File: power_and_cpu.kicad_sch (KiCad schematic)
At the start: 242 parts, among them J1 CPU1 USB, J10 AUX GPIO 1, J11 CAN2 PLUG, J12 Conn_01x06, J13 ADC AUX 2, J14 AUX GPIO 2, J15 AUX Encoder, J17 CAN Output, J2 CAN Input, J21 Power Input, J3 Encoder 1, J4 Encoder 2, J5 Conn_01x06, J6 CPU2 USB, J7 Conn_01x02, J9 ADC AUX 1, Q7 Q_NMOS_GSD, SW1 SW_MEC_5G, SW2 SW_MEC_5G, SW3 CONFIG SWITCH, U10 SN74LVC1G07QDCKTQ1, U11 TLV1117LV33DCYR, U12 W25Q128JVSIQ, U13 W25Q128JVSIQ, U15 RP2040, U16 ADC081S021CISD/NOPB, U17 isolator, U18 MCP2515-xSO, U19 RP2040, U23 SN74LVC1G07QDCKTQ1, U24 MT2492, U25 NCP1117-5_SOT223, U26 ADC081S021CISD/NOPB, U27 USBLC6-2P6, U28 USBLC6-2P6, U29 USBLC6-4SC6, U30 USBLC6-4SC6, U31 USBLC6-4SC6, U32 TLV1117LV33DCYR, U33 TX4139, U34 LTV-208, U6 SN74LVC1G07QDCKTQ1, U9 ADC081S021CISD/NOPB, Y1 12MHz, Y2 12MHz, Y3 16MHz

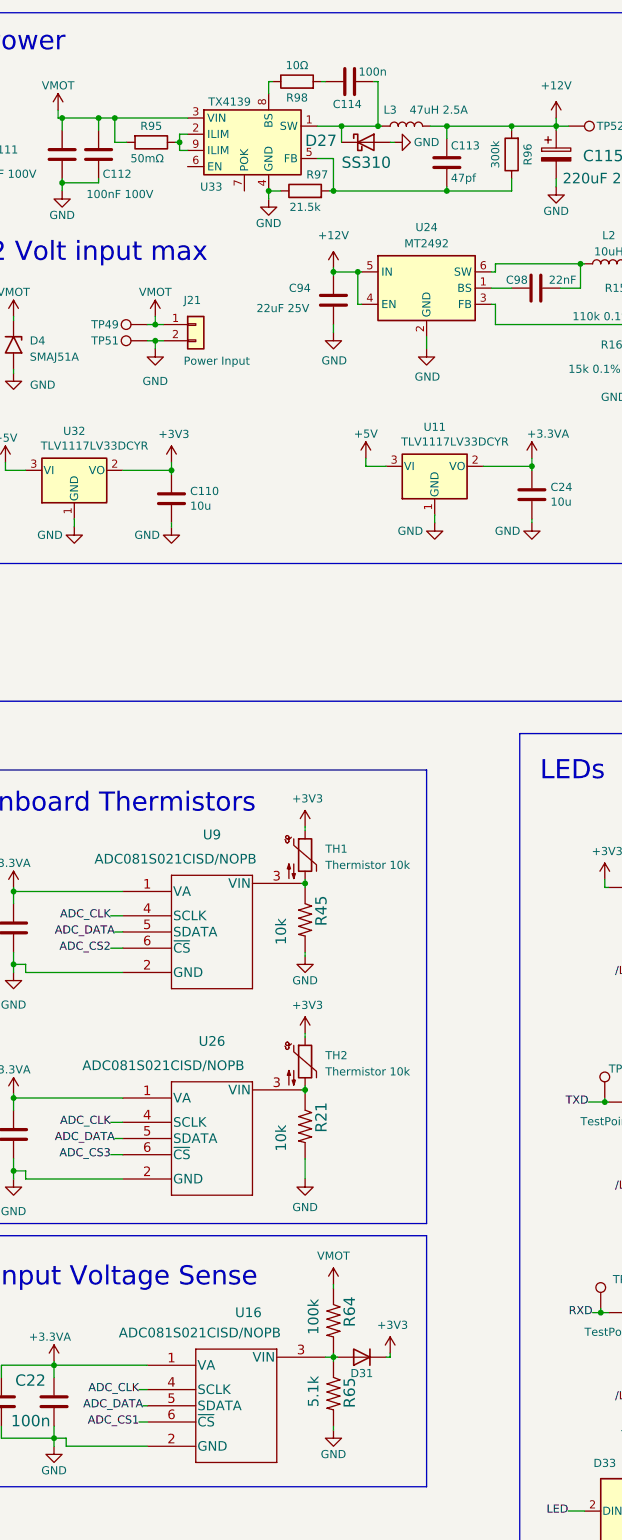
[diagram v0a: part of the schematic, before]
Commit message: Work in progress, starting to place components.
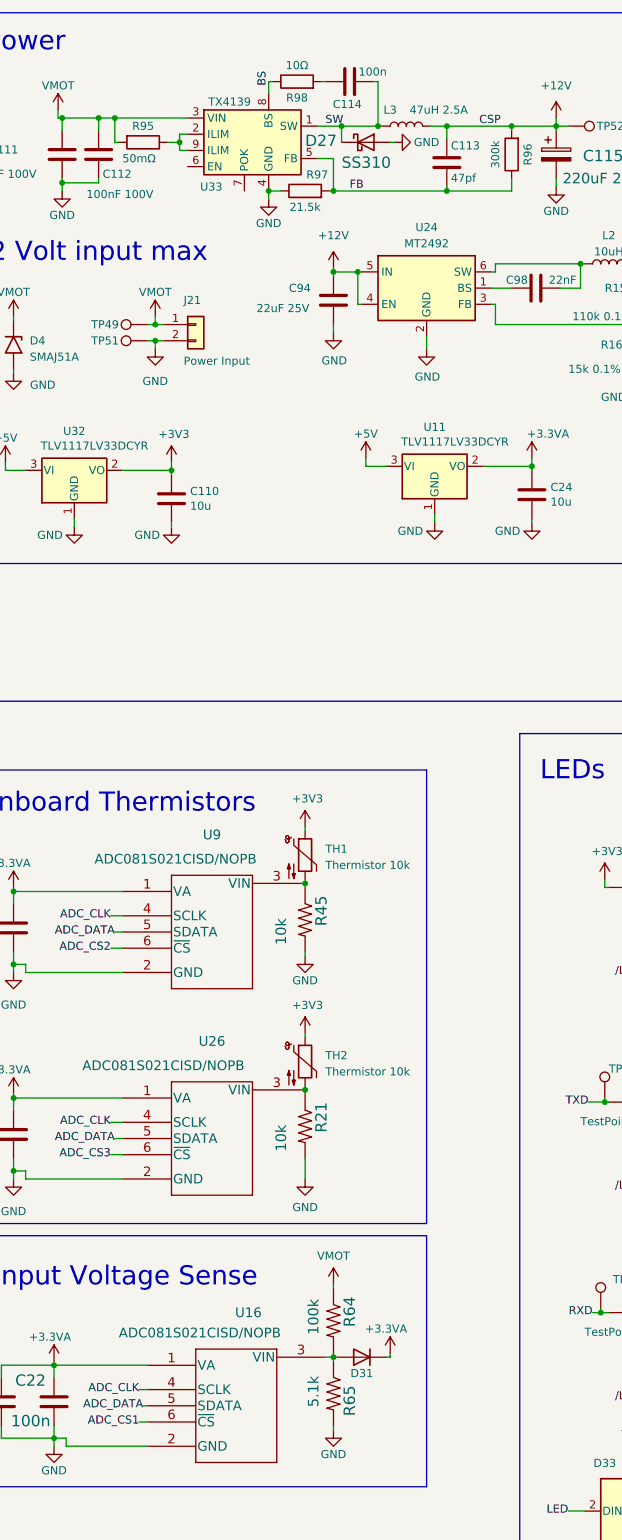
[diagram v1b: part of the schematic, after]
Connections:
- net +3.3VA: now also D31.1 (K)
- net +3V3: no longer D31.1 (K)
- net FB: now reaches C113.2, R96.1, R97.2, U33.5 (FB)
- net SW: now reaches C114.1, D27.1 (K), L3.1, U33.1 (SW)
- net BS: now reaches R98.1, U33.8 (BS)
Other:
- moved on the sheet: R95

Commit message: Work in progress. cleared out old traces in layout and starting fresh
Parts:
- removed U10: SN74LVC1G07QDCKTQ1, Package_TO_SOT_SMD:SOT-353_SC-70-5, symbol acorn-motherboard:SN74LVC1G07QDCKTQ1
- added C119: 0.1uF, Capacitor_SMD:C_0603_1608Metric, symbol Device:C
- added C26: 47uF 63V solid, Capacitor_THT:CP_Radial_D8.0mm_P3.50mm, symbol Device:C_Polarized
- added U10: TXS0101DCKR, Package_TO_SOT_SMD:SOT-363_SC-70-6, symbol MotorBuck:level_shifter
- added U3, U43: USBLC6-4SC6, Package_TO_SOT_SMD:SOT-23-6, symbol Power_Protection:USBLC6-4SC6
- C95: value 22uF 6.3v -> 47uF 10v; footprint Capacitor_SMD:C_0603_1608Metric -> Capacitor_SMD:C_0805_2012Metric
- C96: footprint Capacitor_SMD:C_0603_1608Metric -> Capacitor_SMD:C_0805_2012Metric
- FB2: footprint (none) -> Inductor_SMD:L_0603_1608Metric
- U33: footprint Package_SO:SOIC-8_3.9x4.9mm_P1.27mm -> Package_SO:SOIC-8-1EP_3.9x4.9mm_P1.27mm_EP2.29x3mm_ThermalVias
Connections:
- net +12V: no longer D37.1 (K)
- net +3V3: now also R77.1, U10.1 (VCCA), U10.5 (OE), U3.5 (VBUS), U43.5 (VBUS); no longer D33.3 (VDD), D34.3 (VDD), D35.3 (VDD)
- net +5V: now also D33.3 (VDD), D34.3 (VDD), D35.3 (VDD), D37.1 (K), C119.1, U10.6 (VCCB)
- net CANH0_P: no longer D1.2 (I/O1), J17.5 (Pin_5), J2.5 (Pin_5), TP60.1, U17.7 (CANH)
- net CANL0_N: no longer D1.3 (I/O2), J17.8 (Pin_8), J2.8 (Pin_8), TP56.1, U17.6 (CANL)
- net ESTOP_SWITCH_IN: now also D32.1 (A1), Q7.1 (G)
- net ESTOP_SWITCH_OUT: no longer D32.1 (A1), Q7.1 (G)
- net GND: now also C119.2, C26.2, U10.2 (GND), U3.2 (GND), U43.2 (GND); no longer D41.1 (K)
- net GPIO24: now also U43.6 (I/O4)
- net GPIO25: now also U43.4 (I/O3)
- net LED: now also U10.3 (A); no longer D33.2 (DIN)
- net RXI_2: now also U3.4 (I/O3)
- net SWCLK: now also U43.3 (I/O2)
- net SWCLK_2: now also U3.3 (I/O2)
- net SWD: now also U43.1 (I/O1)
- net SWD_2: now also U3.1 (I/O1)
- net TXO_2: now also U3.6 (I/O4)
- net USB_D+: now also U27.6 (I/O1); no longer U27.3 (I/O2)
- net USB_D-: now also U27.4 (I/O2); no longer U27.1 (I/O1)
- net USB_D_2+: now also U28.6 (I/O1); no longer U28.3 (I/O2)
- net USB_D_2-: now also U28.4 (I/O2); no longer U28.1 (I/O1)
- net VMOT: now also C26.1
- net /LED_EN: now also D41.1 (K)
- net at R60.1: now also U27.1 (I/O1); no longer U27.4 (I/O2)
- net at R61.1: now also U27.3 (I/O2); no longer U27.6 (I/O1)
- net at R71.1: now also U28.3 (I/O2); no longer U28.6 (I/O1)
- net at R70.1: now also U28.1 (I/O1); no longer U28.4 (I/O2)
- net +5VP renamed +5V_ISO
- net +5V_ISO: no longer C1.2, C55.2, FB2.1, R48.1, U17.8 (VCC2)
- net CANH1_P renamed CAN1_P
- net CAN1_P: now also D3.3 (I/O2); no longer D3.2 (I/O1)
- net CANL1_N renamed CAN1_N
- net CAN1_N: now also D3.2 (I/O1); no longer D3.3 (I/O2)
- new net: D33.2 (DIN), U10.4 (B)
- new net +5V_ISO_FILT: C1.2, C55.2, FB2.1, R48.1, U17.8 (VCC2)
- new net CAN0_N: D1.3 (I/O2), J17.8 (Pin_8), J2.8 (Pin_8), TP56.1, U17.6 (CANL)
- new net CAN0_P: D1.2 (I/O1), J17.5 (Pin_5), J2.5 (Pin_5), TP60.1, U17.7 (CANH)
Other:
- moved on the sheet: D33, D34, D35, D38, D39, D41, R67, R68, R77, TP1, TP2, TP3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

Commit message: Latest layout updates, with minor schematic changes.
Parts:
- added C121, C122: 1u, Capacitor_SMD:C_0603_1608Metric, symbol Device:C
- added TP22: TestPoint, TestPoint:TestPoint_Keystone_5019_Minature, symbol Connector:TestPoint
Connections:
- net +3.3VA: now also TH1.1, TH2.1
- net +3V3: no longer TH1.1, TH2.1
- net +5V: now also C121.1, C122.1
- net GND: now also C121.2, C122.2
- net at U15.30 (GPIO19): now also TP22.1

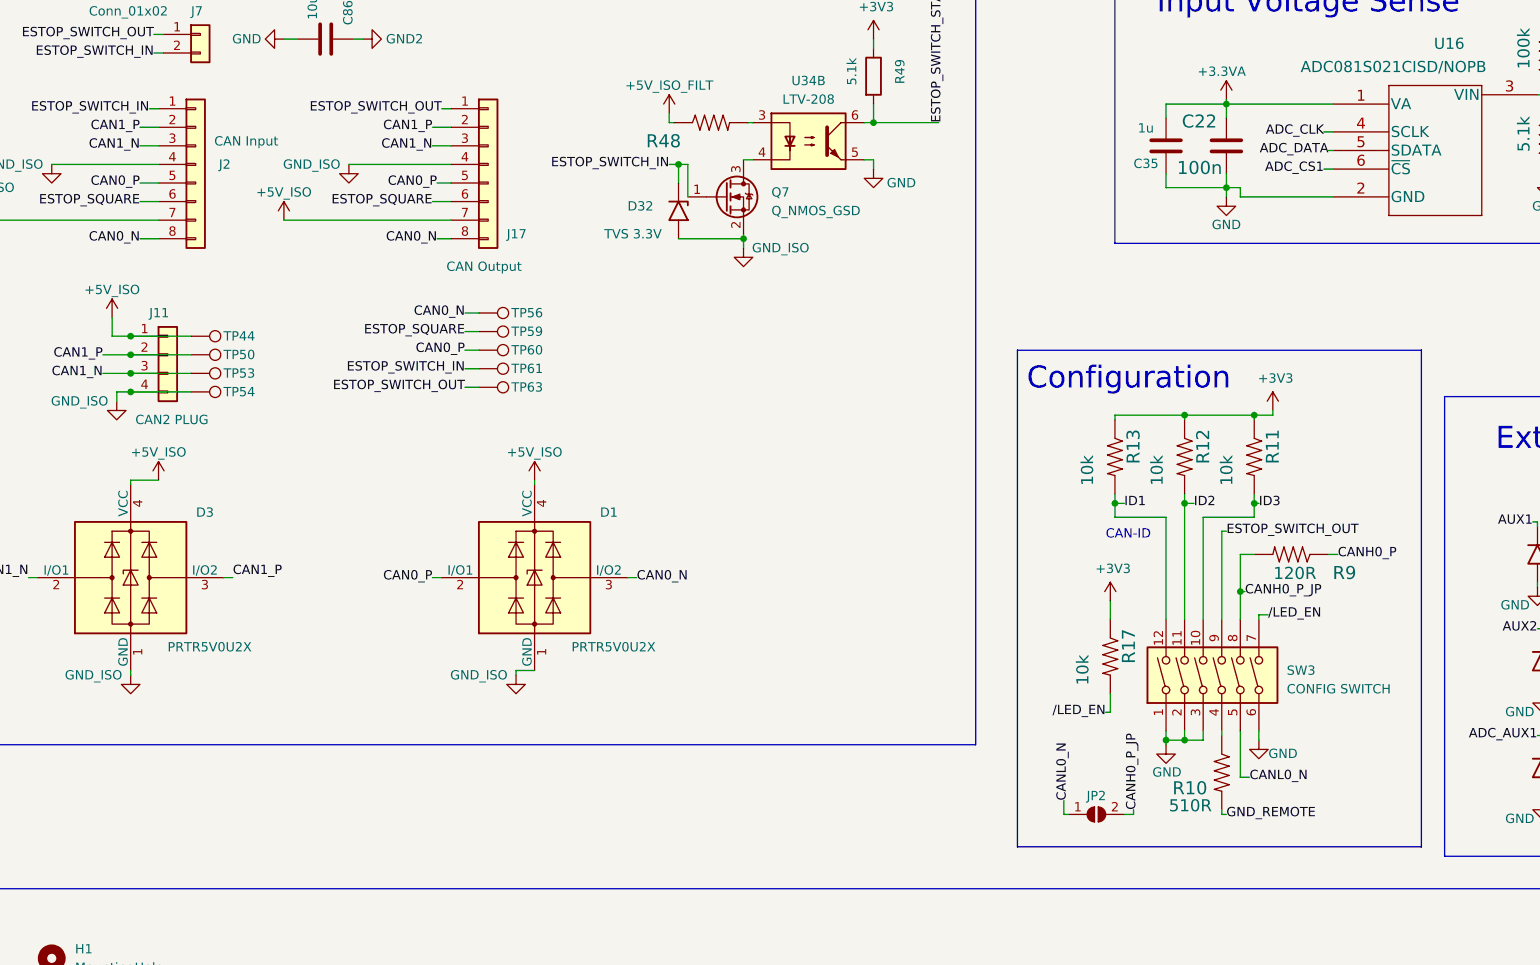
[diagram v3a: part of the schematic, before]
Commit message: initial 100% routing of PCB done with latest updates
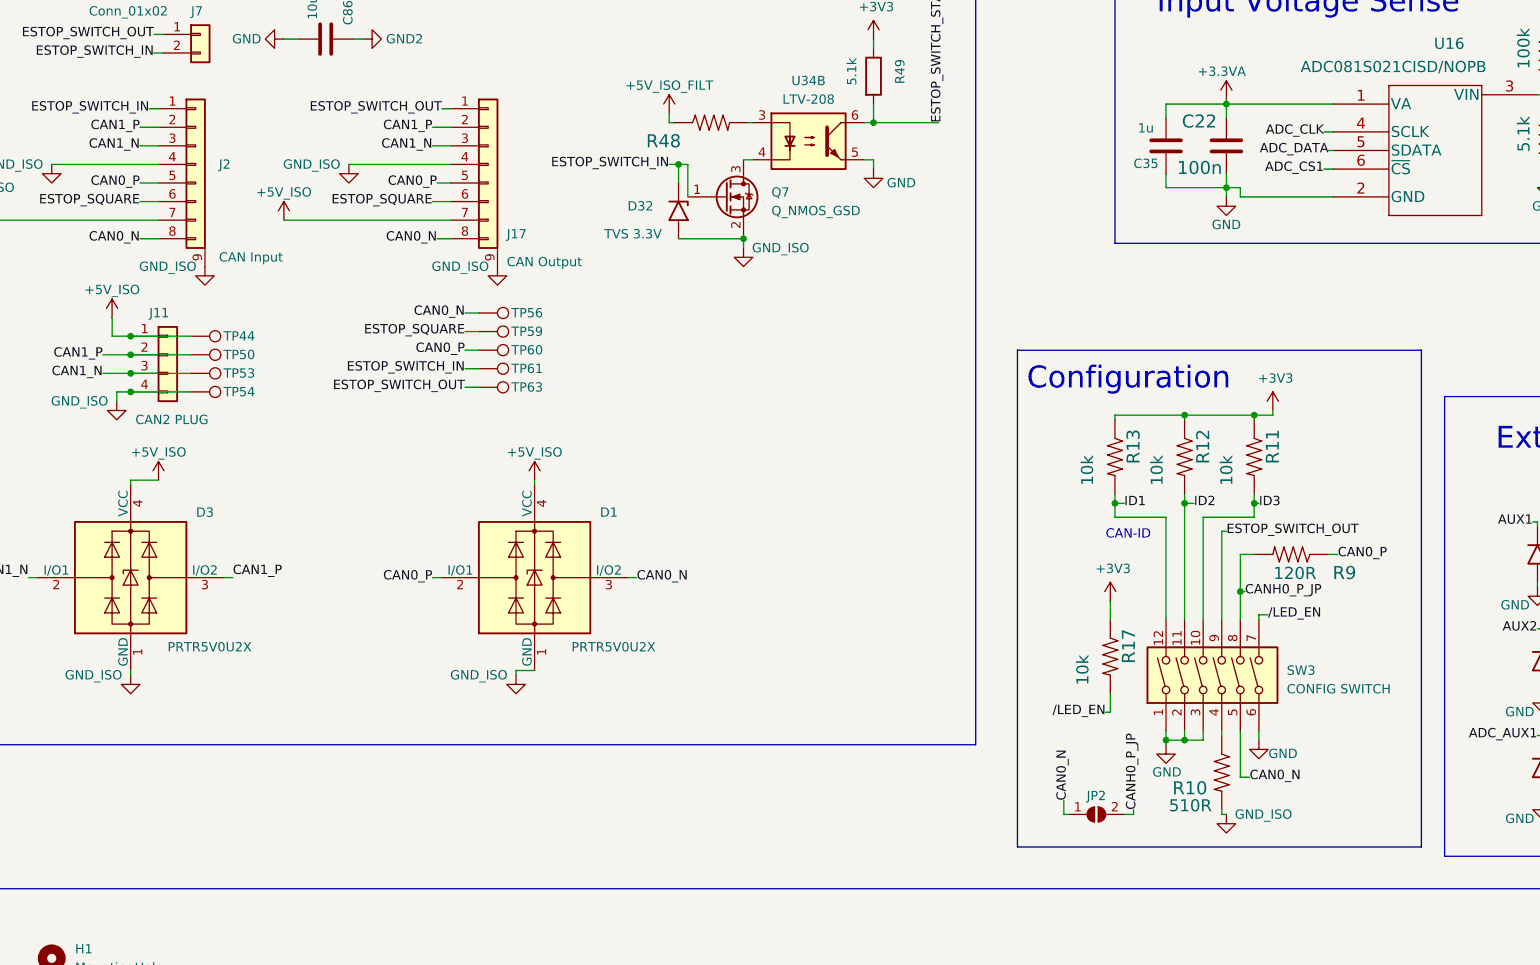
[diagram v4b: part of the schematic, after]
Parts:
- J17, J2: symbol Connector_Generic:Conn_01x08 -> motor_parts:M12_X8_CONNECTOR
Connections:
- net CANH0_P is gone; now on net CAN0_P: R9.1
- net CANL0_N is gone; now on net CAN0_N: JP2.1 (A), SW3.5
- net GND_REMOTE is gone; now on net GND_ISO: R10.2
- net GND_ISO: now also J17.9, J2.9

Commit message: board updates just before adding test points
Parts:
- removed H5, H9: MountingHole, RP2040_minimal:MountingHole_3.9mm_Plastite_#6, symbol Mechanical:MountingHole

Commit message: Nearly complete layout now. Probably a functional design.
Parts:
- added D43: B5819W SL, Diode_SMD:D_SOD-123, symbol Diode:MBR340
- C87, C88, C89, C90, C91, C92, J21: now left out of the parts list
- D4: LCSC C173506 -> C726760
- J10, J13, J14, J9: LCSC C29275 -> C509148
- R42, R51: now not fitted; now left out of the parts list
- R48: value ~ -> 120R; LCSC (none) -> C22787
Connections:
- net +5V: now also D43.1 (K)
- net VBUS: no longer J1.A4 (VBUS), J1.A9 (VBUS), J1.B4 (VBUS), J1.B9 (VBUS), TP40.1, U27.5 (VBUS)
- new net VBUS2: D43.2 (A), J1.A4 (VBUS), J1.A9 (VBUS), J1.B4 (VBUS), J1.B9 (VBUS), TP40.1, U27.5 (VBUS)
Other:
- moved on the sheet: TP40

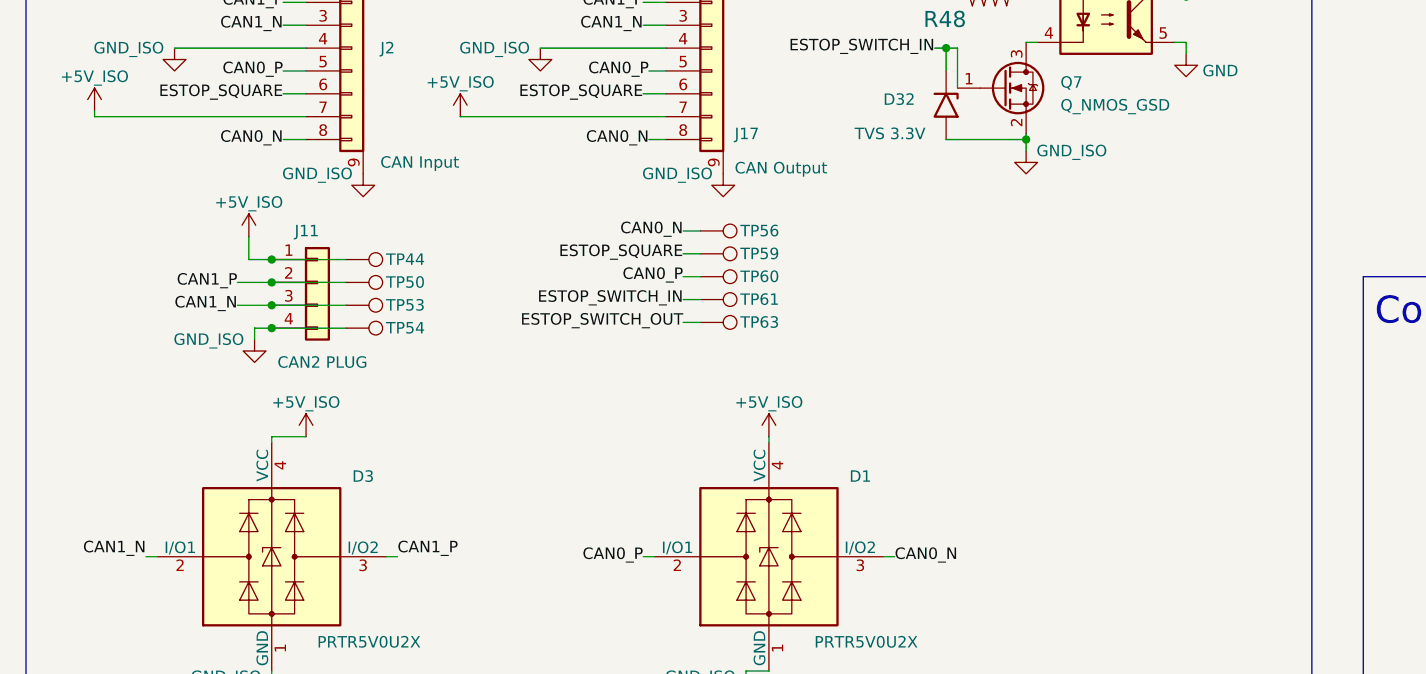
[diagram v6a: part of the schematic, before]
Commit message: Added test points for full bridge and did light clean up on pcb.
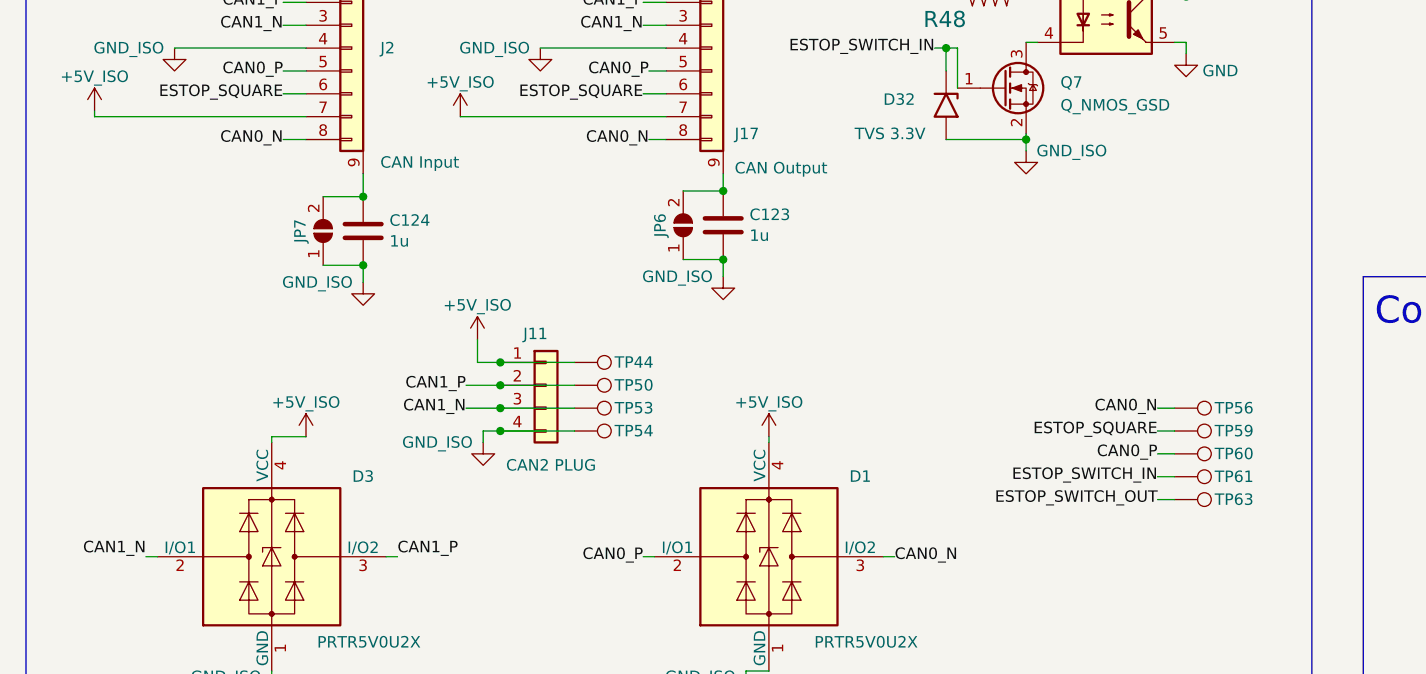
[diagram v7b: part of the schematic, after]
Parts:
- added C123, C124: 1u, Capacitor_SMD:C_0603_1608Metric, symbol Device:C
- added JP6, JP7: SolderJumper_2_Open, Jumper:SolderJumper-2_P1.3mm_Open_RoundedPad1.0x1.5mm, symbol Jumper:SolderJumper_2_Open
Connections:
- net GND_ISO: now also C123.2, C124.2, JP6.1 (A), JP7.1 (A); no longer J17.9, J2.9
- new net: C124.1, J2.9, JP7.2 (B)
- new net: C123.1, J17.9, JP6.2 (B)
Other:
- moved on the sheet: J11, TP44, TP50, TP53, TP54, TP56, TP59, TP60, TP61, TP63
